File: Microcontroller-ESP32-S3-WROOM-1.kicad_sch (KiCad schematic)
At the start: 26 parts, among them Q1 BC817, Q2 BC817, U3 CP2102N-Axx-xQFN20, U4 ESP32-S3-WROOM-1

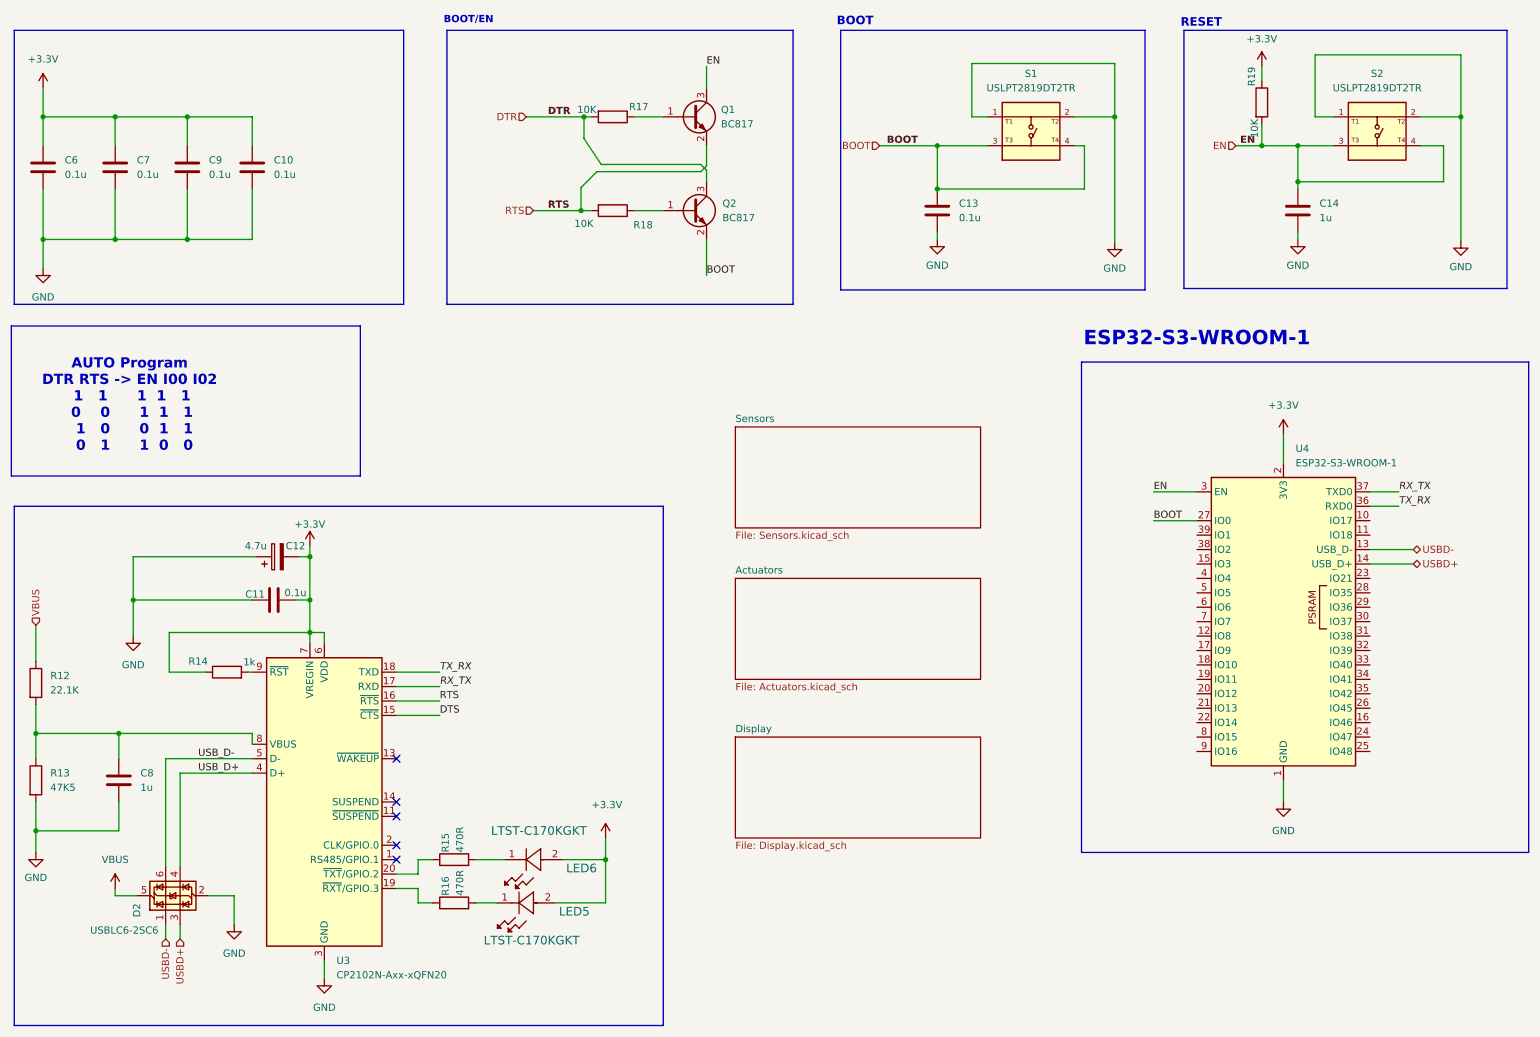
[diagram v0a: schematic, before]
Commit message: feat(sch): add additional wire connections and labels for SDA, SCL, and INT
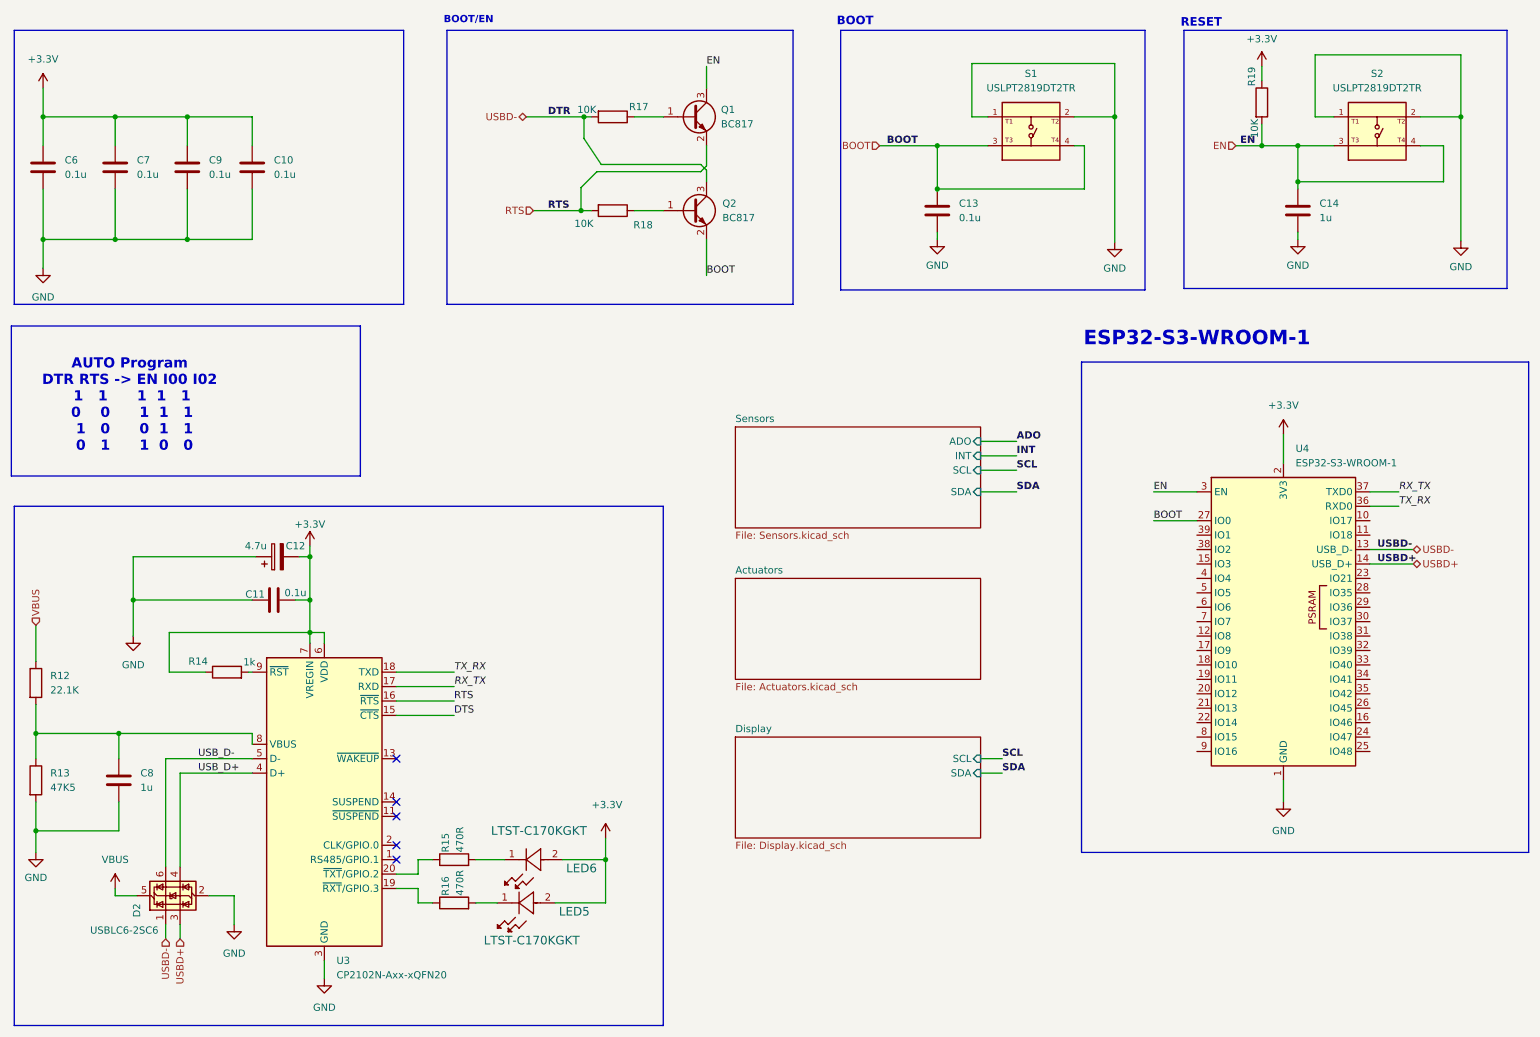
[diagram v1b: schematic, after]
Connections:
- net DTR is gone; now on net USBD-: Q2.3 (C), R17.2
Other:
- sheet Display ports: added SCL, SDA; removed none
- sheet Sensors ports: added ADO, INT, SCL, SDA; removed none
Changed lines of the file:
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@@
 	(wire
 		(pts
+			(xy 185.42 95.25) (xy 191.77 95.25)
+		)
+		(stroke
+			(width 0)
+			(type default)
+		)
+	)
+	(wire
+		(pts
 			(xy 33.02 33.02) (xy 45.72 33.02)
 		)
@@
 	(wire
 		(pts
-			(xy 82.55 130.81) (xy 90.17 130.81)
+			(xy 82.55 130.81) (xy 92.71 130.81)
 		)
 		(stroke
@@
 	(wire
 		(pts
-			(xy 82.55 133.35) (xy 90.17 133.35)
+			(xy 82.55 133.35) (xy 92.71 133.35)
+		)
+		(stroke
+			(width 0)
+			(type default)
+		)
+	)
+	(wire
+		(pts
+			(xy 185.42 92.71) (xy 191.77 92.71)
 		)
 		(stroke
@@
 	(wire
 		(pts
-			(xy 82.55 138.43) (xy 90.17 138.43)
+			(xy 82.55 138.43) (xy 92.71 138.43)
 		)
 		(stroke
@@
 	(wire
 		(pts
-			(xy 82.55 135.89) (xy 90.17 135.89)
+			(xy 82.55 135.89) (xy 92.71 135.89)
 		)
 		(stroke
@@
 	(wire
 		(pts
+			(xy 185.42 99.06) (xy 191.77 99.06)
+		)
+		(stroke
+			(width 0)
+			(type default)
+		)
+	)
+	(wire
+		(pts
 			(xy 19.05 141.605) (xy 33.655 141.605)
 		)
@@
 	(wire
 		(pts
+			(xy 185.42 146.05) (xy 189.23 146.05)
+		)
+		(stroke
+			(width 0)
+			(type default)
+		)
+	)
+	(wire
+		(pts
 			(xy 209.042 33.02) (xy 209.042 55.118)
 		)
@@
 	(wire
 		(pts
+			(xy 185.42 148.59) (xy 189.23 148.59)
+		)
+		(stroke
+			(width 0)
+			(type default)
+		)
+	)
+	(wire
+		(pts
 			(xy 45.72 54.61) (xy 57.15 54.61)
 		)
@@
 	(wire
 		(pts
+			(xy 185.42 90.17) (xy 191.77 90.17)
+		)
+		(stroke
+			(width 0)
+			(type default)
+		)
+	)
+	(wire
+		(pts
 			(xy 36.195 118.11) (xy 57.15 118.11)
 		)
@@
 	)
 	(label "TX_RX"
-		(at 90.17 130.81 0)
+		(at 92.71 130.81 0)
 		(effects
 			(font
@@
 		)
 	)
+	(label "INT"
+		(at 191.77 92.71 0)
+		(effects
+			(font
+				(size 1.27 1.27)
+				(thickness 0.254)
+				(bold yes)
+			)
+			(justify left bottom)
+		)
+	)
 	(label "BOOT"
 		(at 137.16 60.96 0)
@@
 		)
 	)
+	(label "USBD+"
+		(at 255.27 111.76 0)
+		(effects
+			(font
+				(size 1.27 1.27)
+				(thickness 0.254)
+				(bold yes)
+			)
+			(justify left bottom)
+		)
+	)
 	(label "DTS"
-		(at 90.17 138.43 0)
+		(at 92.71 138.43 0)
 		(effects
 			(font
@@
 		)
 	)
+	(label "SDA"
+		(at 191.77 99.06 0)
+		(effects
+			(font
+				(size 1.27 1.27)
+				(thickness 0.254)
+				(bold yes)
+			)
+			(justify left bottom)
+		)
+	)
 	(label "RTS"
-		(at 90.17 135.89 0)
+		(at 92.71 135.89 0)
 		(effects
 			(font
@@
 		)
 	)
+	(label "USBD-"
+		(at 255.27 109.22 0)
+		(effects
+			(font
+				(size 1.27 1.27)
+				(thickness 0.254)
+				(bold yes)
+			)
+			(justify left bottom)
+		)
+	)
+	(label "SCL"
+		(at 189.23 146.05 0)
+		(effects
+			(font
+				(size 1.27 1.27)
+				(thickness 0.254)
+				(bold yes)
+			)
+			(justify left bottom)
+		)
+	)
+	(label "ADO"
+		(at 191.77 90.17 0)
+		(effects
+			(font
+				(size 1.27 1.27)
+				(thickness 0.254)
+				(bold yes)
+			)
+			(justify left bottom)
+		)
+	)
 	(label "RX_TX"
-		(at 90.17 133.35 0)
+		(at 92.71 133.35 0)
 		(effects
 			(font
@@
 		)
 	)
+	(label "SCL"
+		(at 191.77 95.25 0)
+		(effects
+			(font
+				(size 1.27 1.27)
+				(thickness 0.254)
+				(bold yes)
+			)
+			(justify left bottom)
+		)
+	)
 	(label "USB_D+"
 		(at 47.625 148.59 0)
@@
 		)
 	)
+	(label "SDA"
+		(at 189.23 148.59 0)
+		(effects
+			(font
+				(size 1.27 1.27)
+				(thickness 0.254)
+				(bold yes)
+			)
+			(justify left bottom)
+		)
+	)
 	(label "BOOT"
 		(at 168.91 38.1 0)
@@
 		)
 	)
-	(hierarchical_label "DTR"
-		(shape input)
+	(hierarchical_label "USBD-"
+		(shape bidirectional)
 		(at 105.41 33.02 180)
 		(effects
@@
 			)
 		)
+		(pin "SCL" input
+			(at 185.42 146.05 0)
+			(effects
+				(font
+					(size 1.27 1.27)
+				)
+				(justify right)
+			)
+		)
+		(pin "SDA" input
+			(at 185.42 148.59 0)
+			(effects
+				(font
+					(size 1.27 1.27)
+				)
+				(justify right)
+			)
+		)
 		(instances
 			(project "iot_device_pcb"
@@
 			)
 		)
+		(pin "ADO" input
+			(at 185.42 90.17 0)
+			(effects
+				(font
+					(size 1.27 1.27)
+				)
+				(justify right)
+			)
+		)
+		(pin "INT" input
+			(at 185.42 92.71 0)
+			(effects
+				(font
+					(size 1.27 1.27)
+				)
+				(justify right)
+			)
+		)
+		(pin "SCL" input
+			(at 185.42 95.25 0)
+			(effects
+				(font
+					(size 1.27 1.27)
+				)
+				(justify right)
+			)
+		)
+		(pin "SDA" input
+			(at 185.42 99.06 0)
+			(effects
+				(font
+					(size 1.27 1.27)
+				)
+				(justify right)
+			)
+		)

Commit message: fix(sch): resolve unconnected pins and wiring errors in esp32 schematic
Add missing no-connect markers and correct wire coordinates in the
ESP32-S3-WROOM schematic to ensure electrical connectivity integrity
and clear DRC warnings.
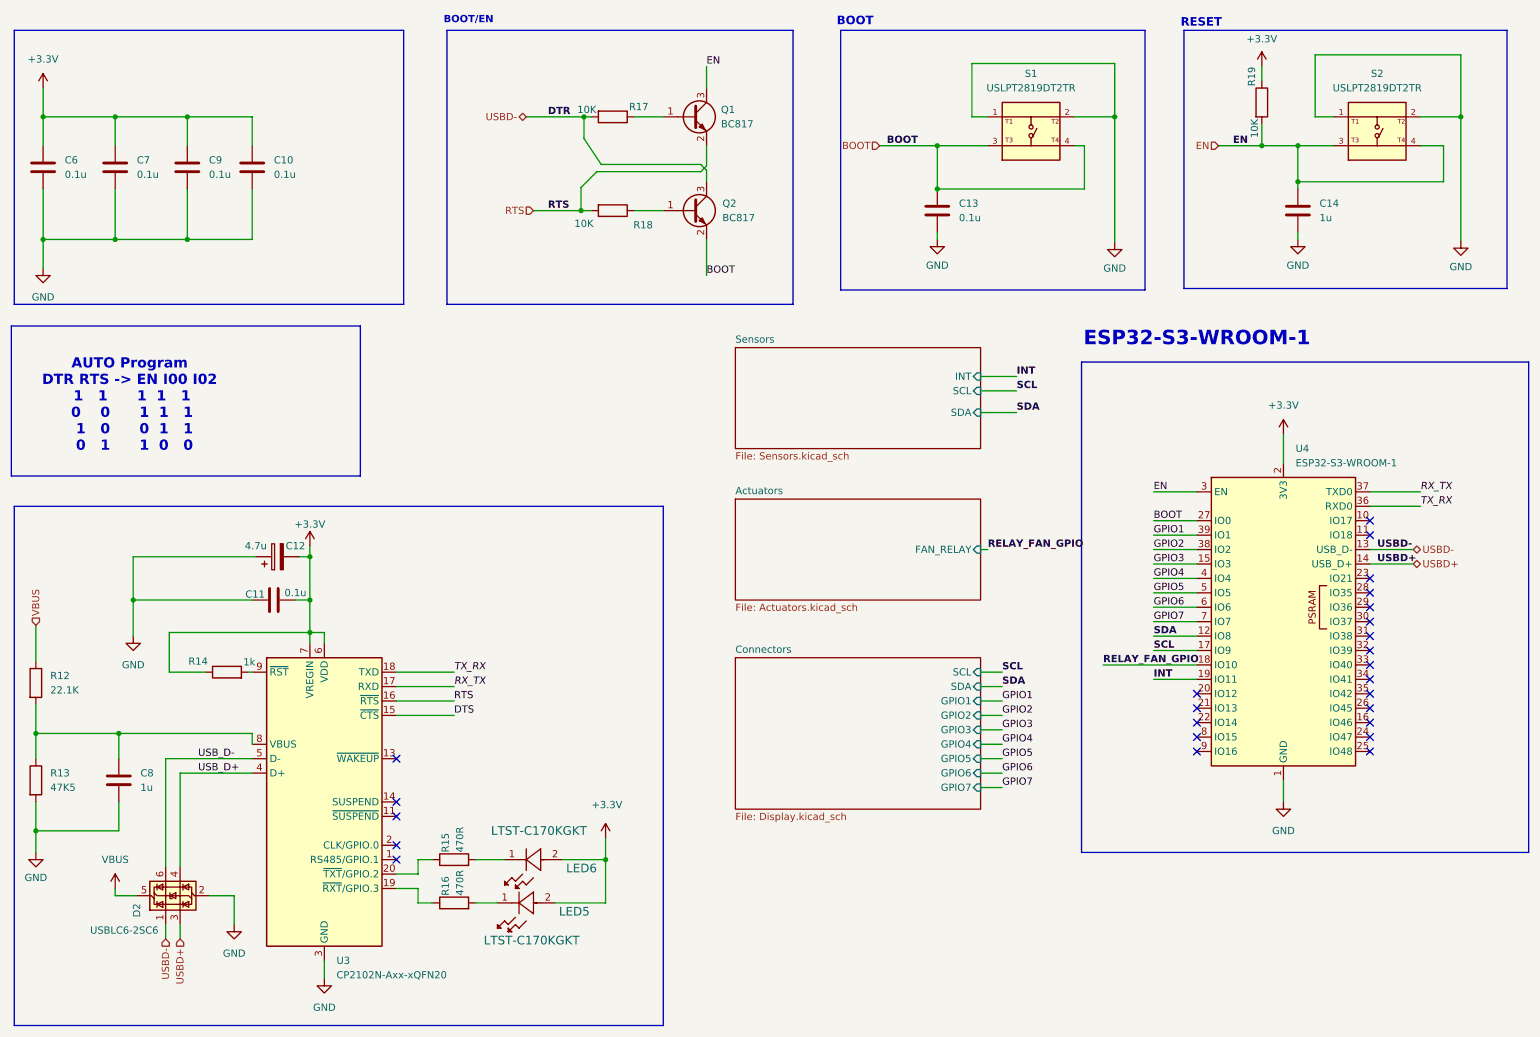
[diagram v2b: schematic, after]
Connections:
- net INT: now also U4.19 (IO11)
- net SCL: now also U4.17 (IO9)
- net SDA: now also U4.12 (IO8)
- net GPIO3: now reaches U4.15 (IO3)
- net RELAY_FAN_GPIO: now reaches U4.18 (IO10)
- net GPIO2: now reaches U4.38 (IO2)
- net GPIO1: now reaches U4.39 (IO1)
- net GPIO4: now reaches U4.4 (IO4)
- net GPIO5: now reaches U4.5 (IO5)
- net GPIO6: now reaches U4.6 (IO6)
- net GPIO7: now reaches U4.7 (IO7)
- no-connect marks 5 -> 25
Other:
- sheet Display renamed Connectors
- sheet Actuators ports: added FAN_RELAY; removed none
- sheet Connectors ports: added GPIO1, GPIO2, GPIO3, GPIO4, GPIO5, GPIO6, GPIO7; removed none
- sheet Sensors ports: added none; removed ADO

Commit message: refactor(sch): remove redundant junctions and wires
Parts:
- removed C10, C7, C9: 0.1u, Capacitor_SMD:C_0805_2012Metric, symbol Device:C
- renumbered C13 to C10, C14 to C11, C8 to C7, C11 to C8, C12 to C9

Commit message: refactor(sch): adjust symbol properties and pin mapping
Update component metadata and pin assignments within the schematic to
improve property management and ensure correct pin numbering. This
includes setting visibility flags for properties and correcting
pin positions for specific symbols.
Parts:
- S1, S2: footprint FootPrints:SW_USLPT2819DT2TR -> USLPT2819DT2TR:SW_USLPT2819DT2TR
